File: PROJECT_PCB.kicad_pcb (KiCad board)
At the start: 4 copper layers, 83 parts, among them J1 SS-52400-003, J2 B2B-PH-K-S_LF__SN_, J3 GSD090012SEU, J4 Conn_01x04_Pin, J5 Conn_01x05_Pin, Q1 TEMT6000X01, Q2 BC817, Q3 BC817, U1 MCP73871, U2 USBLC6-2SC6, U3 ESP32-C3-WROOM-02, U4 CP2102N-Axx-xQFN20, U5 W25Q16JVSS, U6 BME280, U7 MAX4466EXK

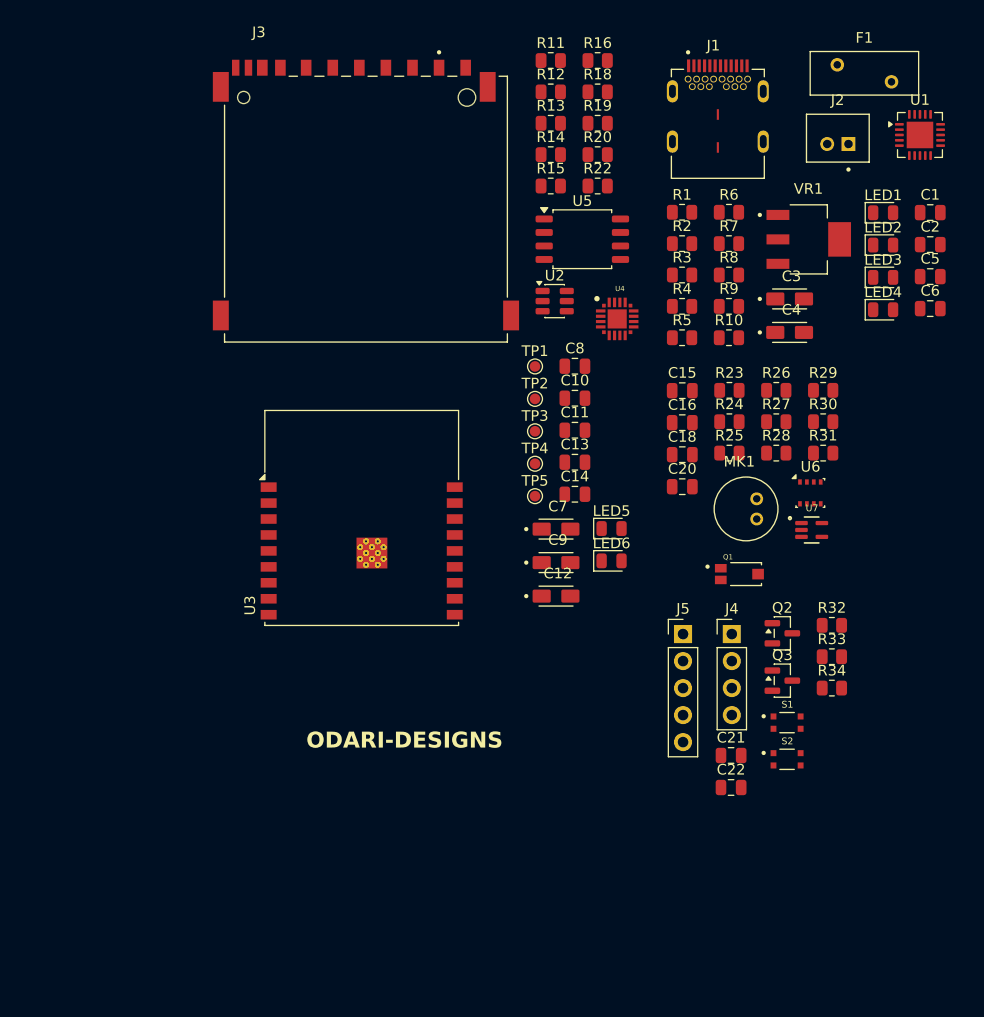
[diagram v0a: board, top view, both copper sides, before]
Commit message: PCB outlining and component placement
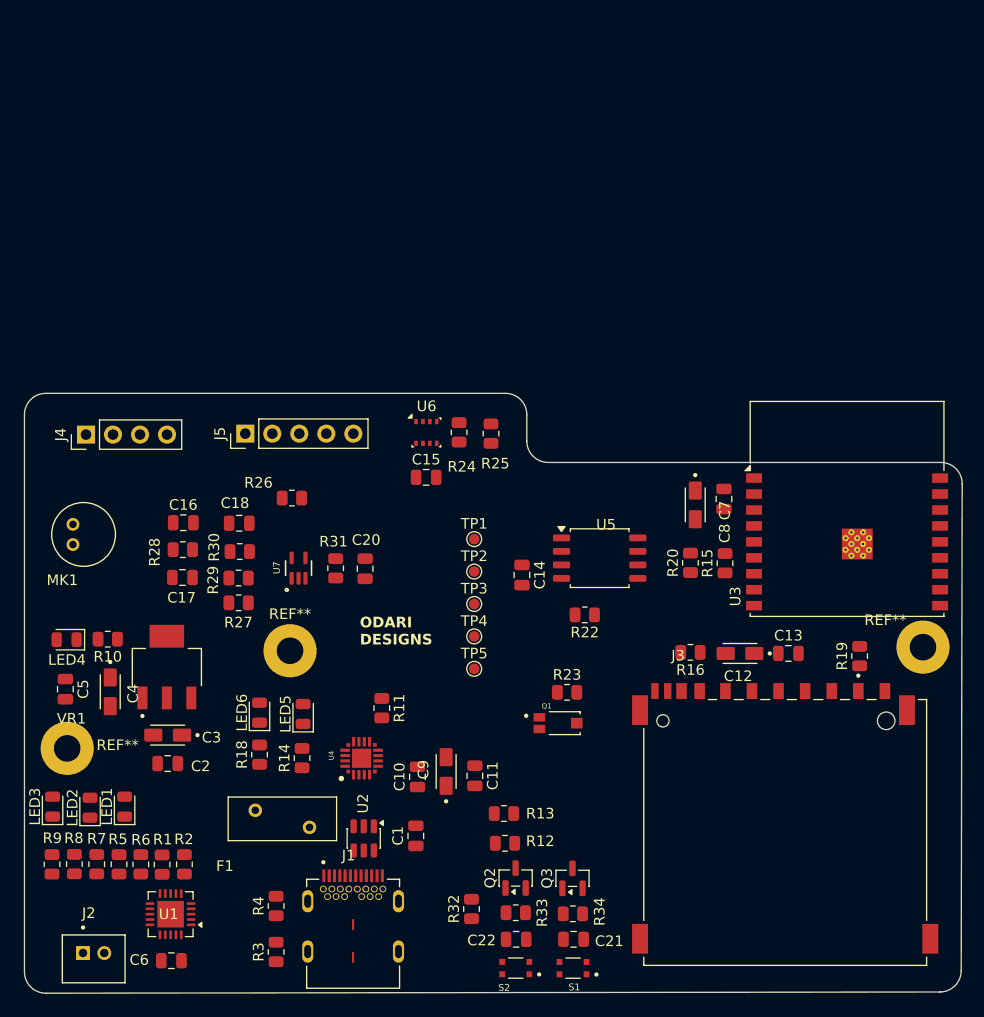
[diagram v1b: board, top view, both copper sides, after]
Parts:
- added C17: 10n, Capacitor_SMD:C_0805_2012Metric, F.Cu at (102.4, 98.3)
- added REF**: MountingHole_2.5mm_Pad, MountingHole:MountingHole_2.5mm_Pad, F.Cu at (172.0, 104.9)
- added REF**: MountingHole_2.5mm_Pad, MountingHole:MountingHole_2.5mm_Pad, F.Cu at (112.5, 105.2)
- added REF**: MountingHole_2.5mm_Pad, MountingHole:MountingHole_2.5mm_Pad, F.Cu at (91.5, 114.4)
- moved J2 104.2 mm to (94.0, 134.2), turned to 180 degrees
- moved U1 101.7 mm to (101.2, 130.0), turned to 180 degrees
- moved C6 94.1 mm to (101.3, 134.4)
- moved LED3 92.6 mm to (90.1, 119.9), turned to 90 degrees
- moved LED2 91.5 mm to (93.7, 120.0), turned to 90 degrees
- moved LED1 90.6 mm to (96.9, 119.9), turned to 90 degrees
- moved C5 90.1 mm to (91.3, 108.8), turned to -90 degrees
- moved F1 87.2 mm to (114.3, 121.8), turned to 180 degrees
- moved C2 86.8 mm to (101.0, 115.8), turned to 180 degrees
- moved J1 83.5 mm to (118.4, 133.5)
- moved R7 83.3 mm to (94.3, 125.3), turned to -90 degrees
- moved LED4 82.8 mm to (91.5, 104.2), turned to 180 degrees
- moved R8 82.8 mm to (92.2, 125.3), turned to -90 degrees
- moved R6 82.6 mm to (98.4, 125.3), turned to 90 degrees
- moved R9 82.5 mm to (90.1, 125.3), turned to 90 degrees
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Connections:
- C20 pad 1: GND -> Net-(U7-IN-)
- MK1 pad OUT: Net-(U7-IN+) -> Net-(C17-Pad1)
- R28 pad 2: Net-(U7-IN+) -> Net-(C17-Pad1)
- R30 pad 1: GND -> Net-(U7-IN-)
- R31 pad 1: GND -> Net-(U7-IN-)
- U7 pad 3: GND -> Net-(U7-IN-)
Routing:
- added copper zone on In1.Cu, net +3.3V
- added copper zone on In1.Cu, net /+5V_USB
- added copper zone on In1.Cu, net /VBUS
- added copper zone on In2.Cu, net GND
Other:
- board outline added: 88.2 x 56.4 mm
- board text added: "ODARI DESIGNS"
- board text removed: "ODARI-DESIGNS"

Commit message: routing pcb
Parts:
- moved REF** 46.7 mm to (125.3, 103.8)
- moved TP4 39.7 mm to (169.4, 106.6)
- moved REF** 25.8 mm to (97.9, 89.4)
- moved REF** 21.9 mm to (106.8, 126.3)
- moved TP3 18.4 mm to (147.9, 97.5)
- moved J4 18.3 mm to (111.5, 83.5)
- moved TP1 18.0 mm to (146.5, 101.4)
- moved TP5 16.9 mm to (138.1, 92.2)
- moved TP2 14.3 mm to (141.1, 106.5)
- moved J5 13.3 mm to (95.0, 83.5)
- moved R16 3.41 mm to (146.7, 105.0)
- moved Q1 1.43 mm to (136.3, 111.7)
- moved R23 1.43 mm to (137.1, 108.8)
- moved J1 1.17 mm to (119.4, 134.1)
- moved U4 1.10 mm to (118.9, 116.4)
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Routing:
- net /MCU_sheet/MISO_DO: track 0.00 -> 71.5 mm
- net /MCU_sheet/SCL: track 0.00 -> 70.6 mm, vias 0 -> 2
- net /MCU_sheet/SDA: track 0.00 -> 70.1 mm, vias 0 -> 2
- net /MCU_sheet/MOSI_DI: track 0.00 -> 62.2 mm
- net /MCU_sheet/CS: track 0.00 -> 44.2 mm, vias 0 -> 2
- net /MCU_sheet/CD_SD: track 0.00 -> 27.0 mm, vias 0 -> 2
- net /MCU_sheet/SCLK: track 0.00 -> 23.6 mm
- net Net-(U5-DO/IO_{1}): track 0.00 -> 7.28 mm
- net Net-(J3-DAT0): track 0.00 -> 6.78 mm
- net Net-(U3-IO6): track 0.00 -> 6.38 mm
- net /USB_DN: track 0.00 -> 4.28 mm
- net /+5V_USB: track 0.00 -> 4.00 mm, vias 0 -> 1
- net /MCU_sheet/USB_D+: track 0.00 -> 3.86 mm
- net /MCU_sheet/USB_D-: track 0.00 -> 3.86 mm
- net /USB_DP: track 0.00 -> 3.77 mm
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- added copper zone on F.Cu, net +3.3V
- added copper zone on F.Cu, net +5V
- added copper zone on F.Cu, net /VBAT
- added copper zone on F.Cu, net GND

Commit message: update pcb layout
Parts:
- removed the REF** at (106.8, 126.3)
- moved F1 1.22 mm to (113.5, 120.9)
- moved R18 0.35 mm to (109.8, 115.3)
- moved LED3 0.11 mm to (90.2, 119.9)
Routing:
- net +5V: track 0.00 -> 33.0 mm, vias 1 -> 4
- net +3.3V: track 0.00 -> 11.1 mm, vias 6 -> 9
- net GND: track 2.11 -> 10.8 mm, vias 10 -> 13
- net /USB_DN: track 4.28 -> 10.2 mm, vias 0 -> 1
- net /USB_DP: track 3.77 -> 9.65 mm, vias 0 -> 1
- net /+5V_USB: track 4.00 -> 8.43 mm, vias 1 -> 3
- net /VBUS: track 0.00 -> 4.42 mm, vias 0 -> 3
- net (no net): track 0.00 -> 1.93 mm

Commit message: update pcb layout
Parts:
- moved C1 0.97 mm to (124.4, 121.7)
- moved C9 0.32 mm to (127.2, 116.2)
- moved C11 0.27 mm to (129.6, 117.0)
- moved R13 0.16 mm to (132.7, 120.4)
- moved C10 0.06 mm to (124.4, 117.0)
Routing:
- net GND: track 10.8 -> 60.1 mm, vias 13 -> 36
- net +3.3V: track 11.1 -> 51.3 mm, vias 9 -> 26
- net /VBUS: track 4.42 -> 7.15 mm, vias 3 -> 4

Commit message: update readme
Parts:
- moved F1 0.55 mm to (114.0, 120.8)
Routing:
- net GND: track 60.1 -> 114.7 mm, vias 36 -> 52
- net +3.3V: track 51.3 -> 102.1 mm, vias 26 -> 36
- net +5V: track 33.0 -> 38.9 mm
- net Net-(U4-VBUS): track 0.00 -> 4.31 mm, vias 0 -> 2
- net /VBAT: track 0.00 -> 3.85 mm, vias 0 -> 2

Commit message: final update on pcb layout
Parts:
- removed REF** (x2): MountingHole_2.5mm_Pad, MountingHole:MountingHole_2.5mm_Pad
- moved F1 0.81 mm to (114.1, 121.6)
- moved R18 0.41 mm to (109.4, 115.2)
- moved Q1 0.14 mm to (136.3, 111.6)
- moved R23 0.14 mm to (137.1, 108.7)
- moved R14 0.09 mm to (113.7, 115.3)
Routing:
- net /MCU_sheet/GPIO18: track 0.00 -> 86.2 mm, vias 0 -> 2
- net /MCU_sheet/GPIO19: track 0.00 -> 80.5 mm, vias 0 -> 2
- net /MCU_sheet/RX_TX: track 0.00 -> 79.9 mm, vias 0 -> 2
- net /MCU_sheet/EN: track 0.00 -> 74.5 mm, vias 0 -> 6
- net /MCU_sheet/TX_RX: track 0.00 -> 72.5 mm, vias 0 -> 2
- net /MCU_sheet/GPIO8: track 0.00 -> 70.6 mm, vias 0 -> 4
- net /MCU_sheet/BOOT: track 0.00 -> 68.9 mm, vias 0 -> 2
- net /MCU_sheet/PHOTO_C: track 0.00 -> 63.5 mm, vias 0 -> 2
- net /MCU_sheet/MIC_OUT: track 0.00 -> 51.2 mm, vias 0 -> 2
- net /MCU_sheet/DTS: track 0.00 -> 41.4 mm, vias 0 -> 2
- net /MCU_sheet/RTS: track 0.00 -> 40.5 mm, vias 0 -> 2
- net Net-(U1-CE): track 0.00 -> 28.6 mm, vias 0 -> 2
- net Net-(J1-VBUSB1): track 0.00 -> 27.8 mm
- net +3.3V: track 102.1 -> 75.9 mm, vias 36 -> 38
- net Net-(U4-VBUS): track 4.31 -> 26.5 mm, vias 2 -> 3
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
